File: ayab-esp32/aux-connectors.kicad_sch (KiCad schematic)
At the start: 27 parts, among them J403 AYAB_I2C, J403 AYAB_UART, J403 USER_I2C, J404 AYAB_SPI, J802 I2C_VBUS, J804 I2C_VBUS, Q801 AO3400A, Q802 AO3400A, Q803 AO3400A, Q804 AO3400A

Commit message: review ZVD P-ch MOSFET and resistors
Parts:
- J403: symbol Library:Conn_01x04 -> ayab-lib:Conn_01x04
- J404: symbol Library:Conn_01x06 -> ayab-lib:Conn_01x06
- J802, J804: symbol Library:Conn_01x03 -> ayab-lib:Conn_01x03
- Q801, Q802, Q803, Q804: symbol Library:AO3400A -> ayab-lib:AO3400A
- R401, R402, R801, R802, R805, R806, R809, R810, R813: symbol Library:R_Small_US -> ayab-lib:R_Small_US
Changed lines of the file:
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@@
     )
   )
-  (symbol (lib_id "Library:R_Small_US") (at 182.88 59.69 0) (unit 1)
+  (symbol (lib_id "ayab-lib:R_Small_US") (at 182.88 59.69 0) (unit 1)
     (in_bom yes) (on_board yes) (dnp no)
     (property "Reference" "R401" (at 181.61 58.42 0)
@@
     )
   )
-  (symbol (lib_id "Library:R_Small_US") (at 210.82 142.24 0) (unit 1)
+  (symbol (lib_id "ayab-lib:R_Small_US") (at 210.82 142.24 0) (unit 1)
     (in_bom yes) (on_board yes) (dnp no)
     (property "Reference" "R401" (at 208.28 140.97 0)
@@
     )
   )
-  (symbol (lib_id "Library:Conn_01x03") (at 93.98 43.18 90) (unit 1)
+  (symbol (lib_id "ayab-lib:Conn_01x03") (at 93.98 43.18 90) (unit 1)
     (in_bom yes) (on_board yes) (dnp no)
     (property "Reference" "J802" (at 90.17 38.1 90)
@@
     )
   )
-  (symbol (lib_id "Library:Conn_01x04") (at 90.17 134.62 0) (unit 1)
+  (symbol (lib_id "ayab-lib:Conn_01x04") (at 90.17 134.62 0) (unit 1)
     (in_bom yes) (on_board yes) (dnp no) (fields_autoplaced)
     (property "Reference" "J403" (at 92.71 134.62 0)
@@
     )
   )
-  (symbol (lib_id "Library:Conn_01x04") (at 124.46 67.31 0) (unit 1)
+  (symbol (lib_id "ayab-lib:Conn_01x04") (at 124.46 67.31 0) (unit 1)
     (in_bom yes) (on_board yes) (dnp no) (fields_autoplaced)
     (property "Reference" "J403" (at 127 67.31 0)
@@
     )
   )
-  (symbol (lib_id "Library:R_Small_US") (at 193.04 59.69 0) (unit 1)
+  (symbol (lib_id "ayab-lib:R_Small_US") (at 193.04 59.69 0) (unit 1)
     (in_bom yes) (on_board yes) (dnp no)
     (property "Reference" "R402" (at 191.77 58.42 0)
@@
     )
   )
-  (symbol (lib_id "Library:R_Small_US") (at 64.77 134.62 270) (unit 1)
+  (symbol (lib_id "ayab-lib:R_Small_US") (at 64.77 134.62 270) (unit 1)
     (in_bom yes) (on_board yes) (dnp no)
     (property "Reference" "R806" (at 62.23 137.16 90)
@@
     )
   )
-  (symbol (lib_id "Library:R_Small_US") (at 168.91 69.85 90) (unit 1)
+  (symbol (lib_id "ayab-lib:R_Small_US") (at 168.91 69.85 90) (unit 1)
     (in_bom yes) (on_board yes) (dnp no)
     (property "Reference" "R810" (at 166.37 67.31 90)
@@
     )
   )
-  (symbol (lib_id "Library:Conn_01x04") (at 254 67.31 0) (unit 1)
+  (symbol (lib_id "ayab-lib:Conn_01x04") (at 254 67.31 0) (unit 1)
     (in_bom yes) (on_board yes) (dnp no) (fields_autoplaced)
     (property "Reference" "J403" (at 256.54 67.31 0)
@@
     )
   )
-  (symbol (lib_id "Library:R_Small_US") (at 63.5 59.69 0) (unit 1)
+  (symbol (lib_id "ayab-lib:R_Small_US") (at 63.5 59.69 0) (unit 1)
     (in_bom yes) (on_board yes) (dnp no)
     (property "Reference" "R402" (at 62.23 58.42 0)
@@
     )
   )
-  (symbol (lib_id "Library:R_Small_US") (at 93.98 59.69 0) (unit 1)
+  (symbol (lib_id "ayab-lib:R_Small_US") (at 93.98 59.69 0) (unit 1)
     (in_bom yes) (on_board yes) (dnp no)
     (property "Reference" "R402" (at 92.71 58.42 0)
@@
     )
   )
-  (symbol (lib_id "Library:Conn_01x03") (at 223.52 43.18 90) (unit 1)
+  (symbol (lib_id "ayab-lib:Conn_01x03") (at 223.52 43.18 90) (unit 1)
     (in_bom yes) (on_board yes) (dnp no)
     (property "Reference" "J804" (at 219.71 38.1 90)
@@
     )
   )
-  (symbol (lib_id "Library:AO3400A") (at 82.55 67.31 270) (unit 1)
+  (symbol (lib_id "ayab-lib:AO3400A") (at 82.55 67.31 270) (unit 1)
     (in_bom yes) (on_board yes) (dnp no)
     (property "Reference" "Q802" (at 76.2 71.12 90)
@@
     )
   )
-  (symbol (lib_id "Library:R_Small_US") (at 64.77 132.08 90) (unit 1)
+  (symbol (lib_id "ayab-lib:R_Small_US") (at 64.77 132.08 90) (unit 1)
     (in_bom yes) (on_board yes) (dnp no)
     (property "Reference" "R805" (at 62.23 129.54 90)
@@
     )
   )
-  (symbol (lib_id "Library:R_Small_US") (at 39.37 69.85 90) (unit 1)
+  (symbol (lib_id "ayab-lib:R_Small_US") (at 39.37 69.85 90) (unit 1)
     (in_bom yes) (on_board yes) (dnp no)
     (property "Reference" "R802" (at 36.83 67.31 90)
@@
     )
   )
-  (symbol (lib_id "Library:R_Small_US") (at 223.52 59.69 0) (unit 1)
+  (symbol (lib_id "ayab-lib:R_Small_US") (at 223.52 59.69 0) (unit 1)
     (in_bom yes) (on_board yes) (dnp no)
     (property "Reference" "R402" (at 222.25 58.42 0)
@@
     )
   )
-  (symbol (lib_id "Library:R_Small_US") (at 101.6 59.69 0) (unit 1)
+  (symbol (lib_id "ayab-lib:R_Small_US") (at 101.6 59.69 0) (unit 1)
     (in_bom yes) (on_board yes) (dnp no)
     (property "Reference" "R402" (at 100.33 58.42 0)
@@
     )
   )
-  (symbol (lib_id "Library:R_Small_US") (at 231.14 59.69 0) (unit 1)
+  (symbol (lib_id "ayab-lib:R_Small_US") (at 231.14 59.69 0) (unit 1)
     (in_bom yes) (on_board yes) (dnp no)
     (property "Reference" "R402" (at 229.87 58.42 0)
@@
     )
   )
-  (symbol (lib_id "Library:R_Small_US") (at 210.82 127 0) (unit 1)
+  (symbol (lib_id "ayab-lib:R_Small_US") (at 210.82 127 0) (unit 1)
     (in_bom yes) (on_board yes) (dnp no)
     (property "Reference" "R401" (at 208.28 125.73 0)
@@
     )
   )
-  (symbol (lib_id "Library:R_Small_US") (at 39.37 64.77 90) (unit 1)
+  (symbol (lib_id "ayab-lib:R_Small_US") (at 39.37 64.77 90) (unit 1)
     (in_bom yes) (on_board yes) (dnp no)
     (property "Reference" "R801" (at 36.83 62.23 90)
@@
     )
   )
-  (symbol (lib_id "Library:R_Small_US") (at 203.2 135.89 90) (unit 1)
+  (symbol (lib_id "ayab-lib:R_Small_US") (at 203.2 135.89 90) (unit 1)
     (in_bom yes) (on_board yes) (dnp no)
     (property "Reference" "R813" (at 199.39 134.62 90)
@@
     )
   )
-  (symbol (lib_id "Library:R_Small_US") (at 168.91 64.77 90) (unit 1)
+  (symbol (lib_id "ayab-lib:R_Small_US") (at 168.91 64.77 90) (unit 1)
     (in_bom yes) (on_board yes) (dnp no)
     (property "Reference" "R809" (at 166.37 62.23 90)
@@
     )
   )
-  (symbol (lib_id "Library:Conn_01x06") (at 228.6 135.89 0) (unit 1)
+  (symbol (lib_id "ayab-lib:Conn_01x06") (at 228.6 135.89 0) (unit 1)
     (in_bom yes) (on_board yes) (dnp no) (fields_autoplaced)
     (property "Reference" "J404" (at 231.14 135.89 0)
@@
     )
   )
-  (symbol (lib_id "Library:AO3400A") (at 73.66 62.23 270) (unit 1)
+  (symbol (lib_id "ayab-lib:AO3400A") (at 73.66 62.23 270) (unit 1)
     (in_bom yes) (on_board yes) (dnp no)
     (property "Reference" "Q801" (at 67.31 66.04 90)
@@
     )
   )
-  (symbol (lib_id "Library:AO3400A") (at 203.2 62.23 270) (unit 1)
+  (symbol (lib_id "ayab-lib:AO3400A") (at 203.2 62.23 270) (unit 1)
     (in_bom yes) (on_board yes) (dnp no)
     (property "Reference" "Q803" (at 196.85 66.04 90)
@@
     )
   )
-  (symbol (lib_id "Library:R_Small_US") (at 53.34 59.69 0) (unit 1)
+  (symbol (lib_id "ayab-lib:R_Small_US") (at 53.34 59.69 0) (unit 1)
     (in_bom yes) (on_board yes) (dnp no)
     (property "Reference" "R401" (at 52.07 58.42 0)
@@
     )
   )
-  (symbol (lib_id "Library:AO3400A") (at 212.09 67.31 270) (unit 1)
+  (symbol (lib_id "ayab-lib:AO3400A") (at 212.09 67.31 270) (unit 1)
     (in_bom yes) (on_board yes) (dnp no)
     (property "Reference" "Q804" (at 205.74 71.12 90)

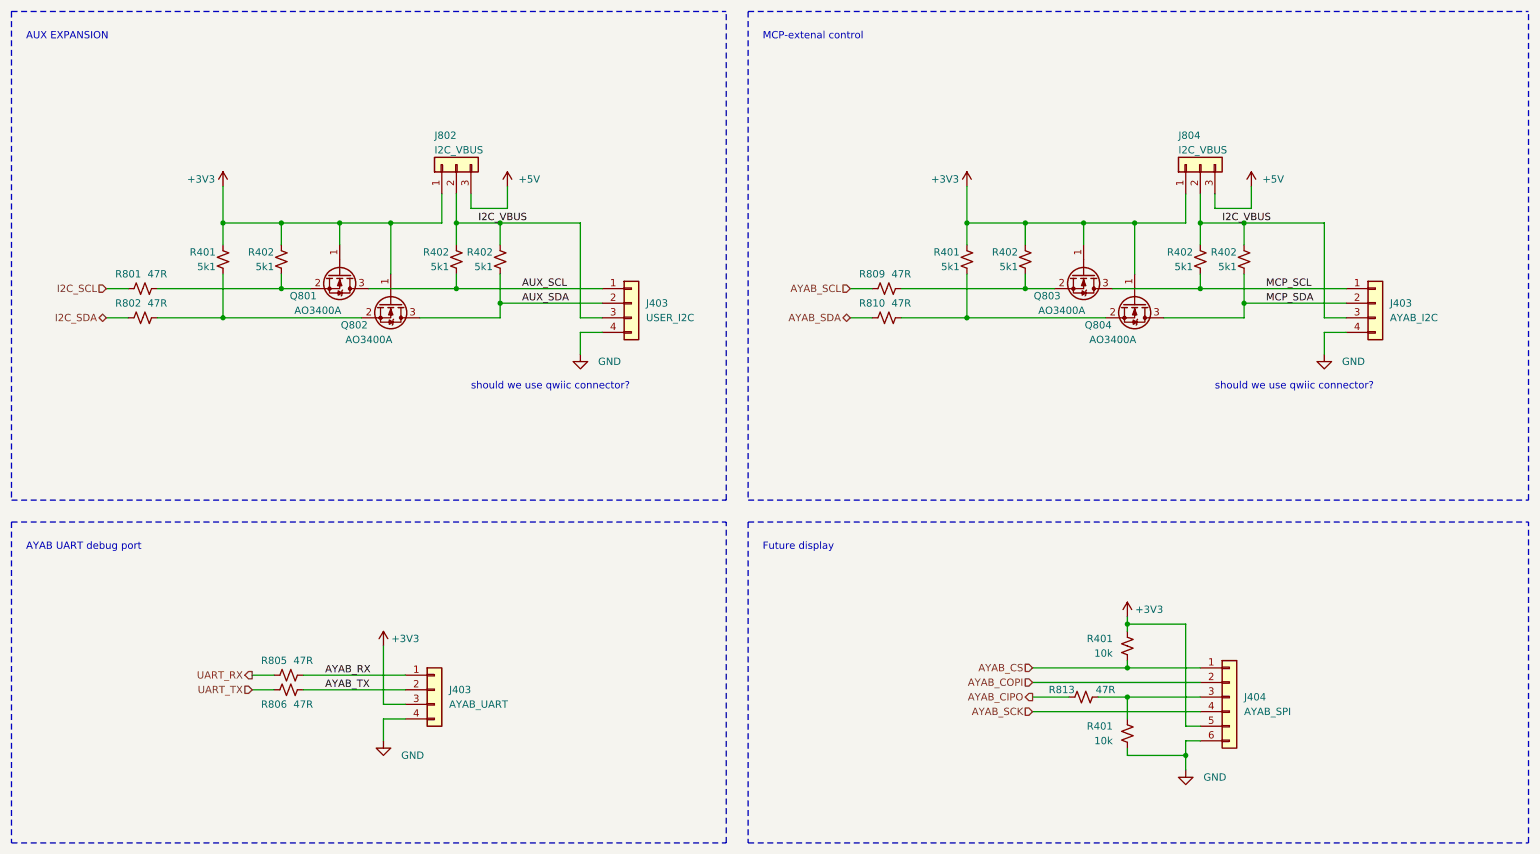
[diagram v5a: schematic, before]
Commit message: first draft layout DRC clean
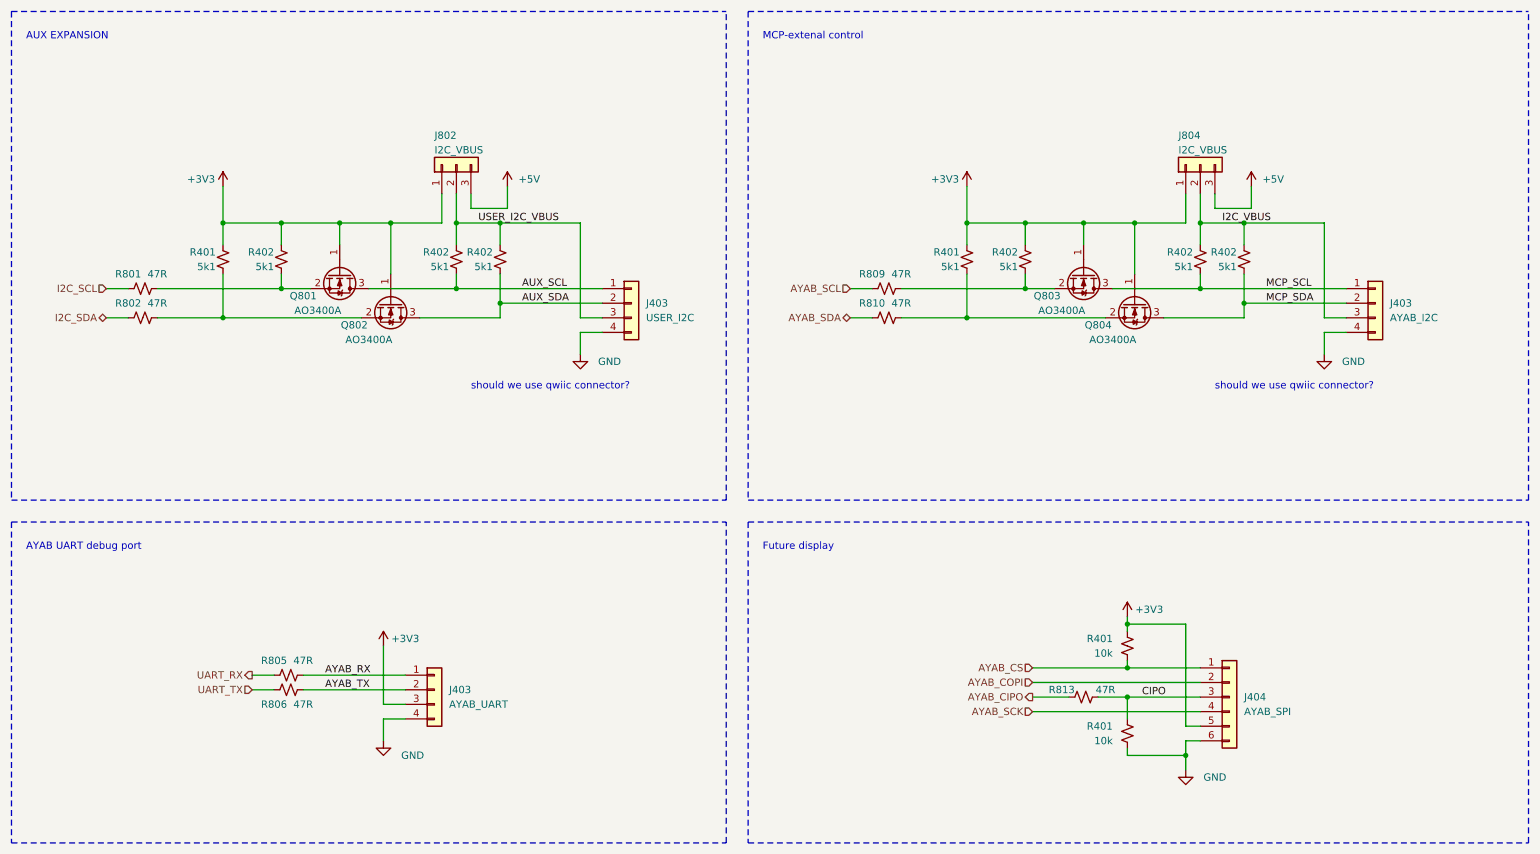
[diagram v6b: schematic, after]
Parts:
- J403: footprint Connector_PinHeader_2.54mm:PinHeader_1x04_P2.54mm_Vertical -> Connector_PinHeader_2.54mm:PinHeader_1x04_P2.54mm_Horizontal
- J403: footprint Connector_PinSocket_2.54mm:PinSocket_1x04_P2.54mm_Vertical -> Connector_PinHeader_2.54mm:PinHeader_1x04_P2.54mm_Horizontal
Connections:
- net I2C_VBUS: no longer J403.3 (Pin_3), J802.2 (Pin_2), R402.1, R402.1
- net CIPO: now reaches J404.3 (Pin_3), R401.1, R813.2
- new net USER_I2C_VBUS: J403.3 (Pin_3), J802.2 (Pin_2), R402.1, R402.1
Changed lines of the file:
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@@
+    (effects (font (size 1.27 1.27)) (justify left bottom))
+  )
+  (label "CIPO" (at 213.36 135.89 0) (fields_autoplaced)
     (effects (font (size 1.27 1.27)) (justify left bottom))
   )
@@
     (effects (font (size 1.27 1.27)) (justify left bottom))
   )
-  (label "I2C_VBUS" (at 97.79 53.34 0) (fields_autoplaced)
+  (label "USER_I2C_VBUS" (at 97.79 53.34 0) (fields_autoplaced)
     (effects (font (size 1.27 1.27)) (justify left bottom))
   )
@@
       (effects (font (size 1.27 1.27)) (justify left))
     )
-    (property "Footprint" "Connector_PinHeader_2.54mm:PinHeader_1x04_P2.54mm_Vertical" (at 90.17 134.62 0)
+    (property "Footprint" "Connector_PinHeader_2.54mm:PinHeader_1x04_P2.54mm_Horizontal" (at 90.17 134.62 0)
       (effects (font (size 1.27 1.27)) hide)
     )
@@
       (effects (font (size 1.27 1.27)) (justify left))
     )
-    (property "Footprint" "Connector_PinSocket_2.54mm:PinSocket_1x04_P2.54mm_Vertical" (at 254 67.31 0)
-      (effects (font (size 1.27 1.27)) hide)
-    )
+    (property "Footprint" "Connector_PinHeader_2.54mm:PinHeader_1x04_P2.54mm_Horizontal" (at 254 67.31 0)
+      (effects (font (size 1.27 1.27)) hide)
+    )

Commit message: revise connector positions
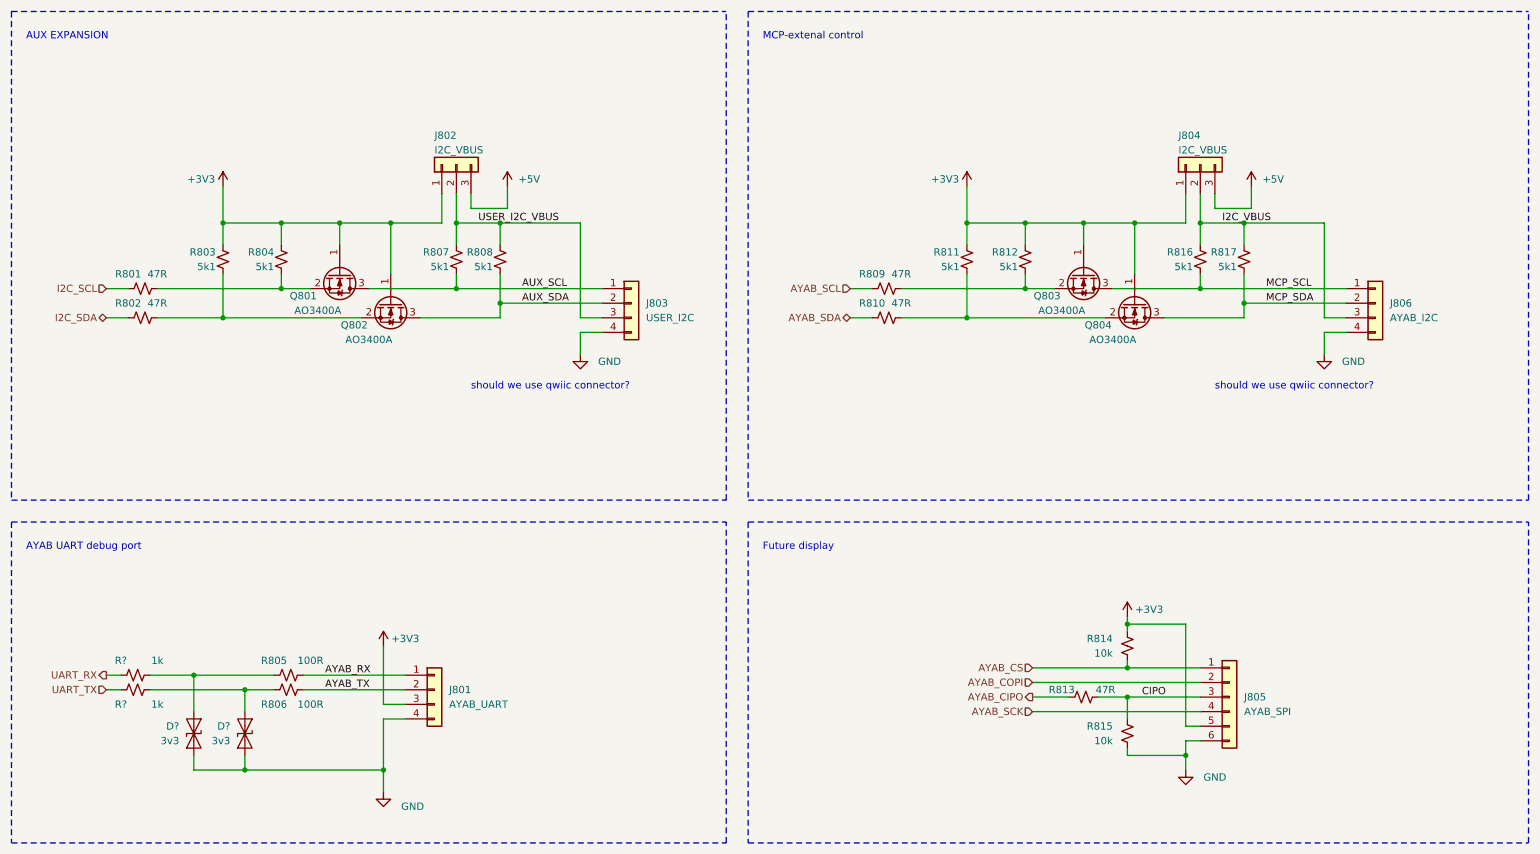
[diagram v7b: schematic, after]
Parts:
- added D? (x2): 3v3, Diode_SMD:D_SOD-923, symbol Diode:ESD9B3.3ST5G
- added R? (x2): 1k, Resistor_SMD:R_0603_1608Metric, symbol ayab-lib:R_Small_US
- J801, J806: renamed from J403; LCSC ID C3029334 -> C7501292; OEM XUNPU -> Megastar; OEM PN WAFER-SH1.0-4PLB -> ZX-PZ2.54-1-4PWZ
- J802, J804: now left out of the parts list
- R805, R806: value 47R -> 100R
- renumbered J403 to J803, J404 to J805, R401 to R803, R402 to R804, R402 to R807, R402 to R808, R401 to R811, R402 to R812, R401 to R814, R401 to R815, R402 to R816, R402 to R817
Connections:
- net GND: now also D?.1 (A1), D?.1 (A1)
- net UART_RX: now also R?.1; no longer R805.1
- net UART_TX: now also R?.2; no longer R806.2
- new net: D?.2 (A2), R806.2, R?.1
- new net: D?.2 (A2), R805.1, R?.2

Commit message: production files
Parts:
- removed D? (x2): 3v3, Diode_SMD:D_SOD-923, symbol Diode:ESD9B3.3ST5G
- removed R805, R806: 100R, Resistor_SMD:R_0603_1608Metric, symbol ayab-lib:R_Small_US
- R818, R819: renamed from R?; value 1k -> 47R
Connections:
- net AYAB_RX: now also R818.2
- net AYAB_TX: now also R819.1
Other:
- moved on the sheet: R818, R819
